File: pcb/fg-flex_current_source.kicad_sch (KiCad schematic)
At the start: 0 parts

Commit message: current sources added
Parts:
- added C13, C14: 0.1uF, Capacitor_THT:C_Disc_D5.1mm_W3.2mm_P5.00mm, symbol Device:C_Small
- added C15: 2.2nF, Capacitor_THT:C_Disc_D5.1mm_W3.2mm_P5.00mm, symbol Device:C_Small
- added Q1: BC547, Package_TO_SOT_THT:TO-92, symbol Transistor_BJT:BC547
- added Q2, Q3: IRF9540N, Package_TO_SOT_THT:TO-220-3_Vertical, symbol Transistor_FET:IRF9540N
- added R10: 0.1R, Resistor_THT:R_Axial_DIN0516_L15.5mm_D5.0mm_P20.32mm_Horizontal, symbol Device:R_Small
- added R11, R4, R5, R6, R7: 1k, Resistor_THT:R_Axial_DIN0207_L6.3mm_D2.5mm_P10.16mm_Horizontal, symbol Device:R_Small
- added R12: 100R, Resistor_THT:R_Axial_DIN0207_L6.3mm_D2.5mm_P10.16mm_Horizontal, symbol Device:R_Small
- added R8, R9: 10k, Resistor_THT:R_Axial_DIN0207_L6.3mm_D2.5mm_P10.16mm_Horizontal, symbol Device:R_Small
- added U6: LM358, Package_DIP:DIP-8_W7.62mm, symbol Amplifier_Operational:LM358
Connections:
- new net: C15.2, R12.1, U6.7
- new net: Q3.1 (G), R12.2
- new net: Q2.2 (D), R10.1
- new net: Q3.3 (S), R10.2, R11.2
- new net -5V: C14.1, U6.4 (V-)
- new net Activation_Signal_FG-Flex: R7.1
- new net GND: C13.2, C14.2, Q1.3 (E), R5.2
- new net I_FG_Flex: Q3.2 (D)
- new net Inv Input U6B: C15.1, R11.1, R6.2, U6.6 (-)
- new net Non-Inv Input U6B: R4.2, R5.1, U6.5 (+)
- new net Q1_Base: Q1.2 (B), R7.2
- new net Q1_Collector: Q1.1 (C), R9.2
- new net Q2_Gate: Q2.1 (G), R8.2, R9.1
- new net U6A Voltage follower: R6.1, U6.1, U6.2 (-)
- new net VCC: C13.1, Q2.3 (S), R4.1, R8.1, U6.8 (V+)
- new net V_{B}: U6.3 (+)

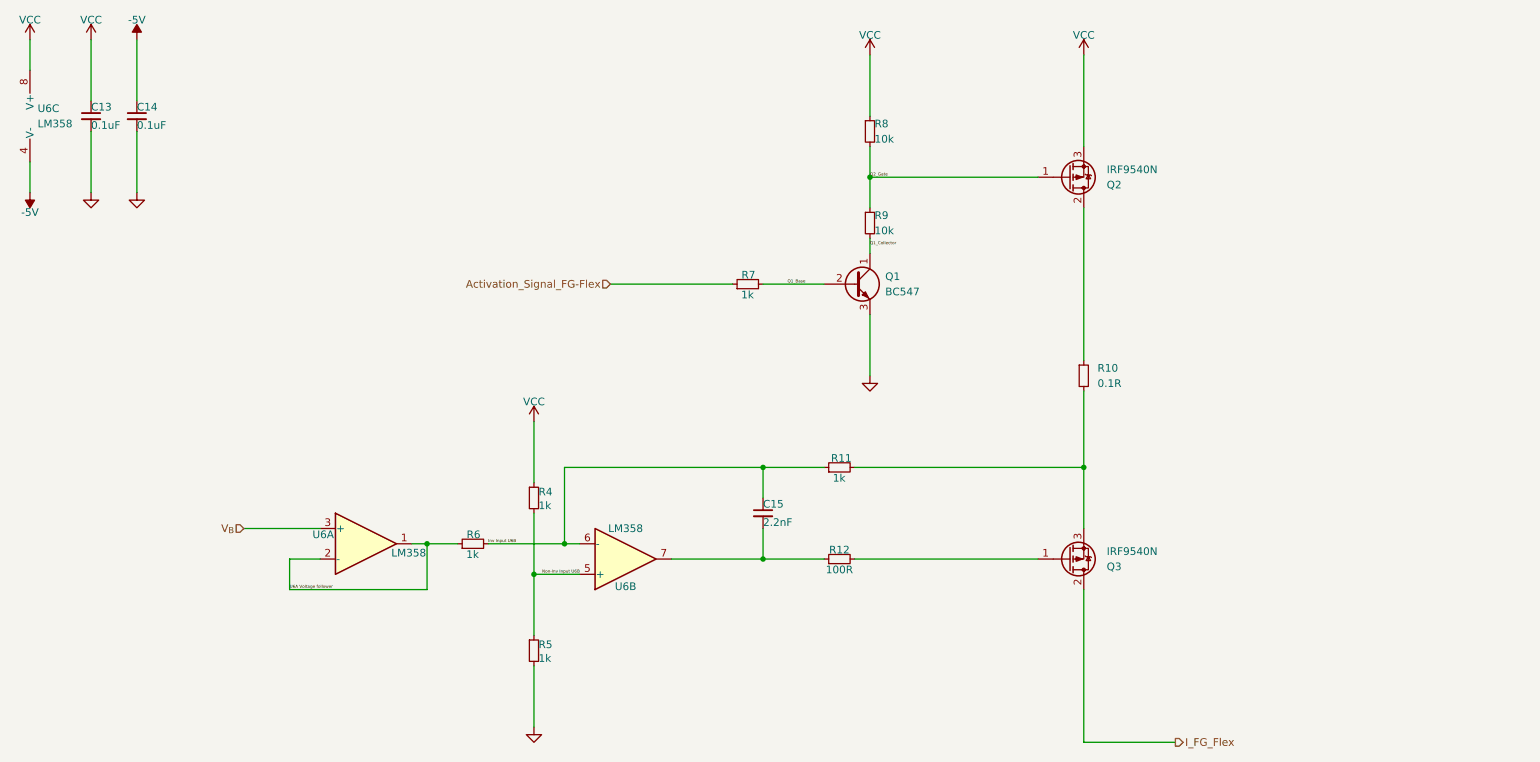
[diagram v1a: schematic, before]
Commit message: shunt measurement changed to different opamp
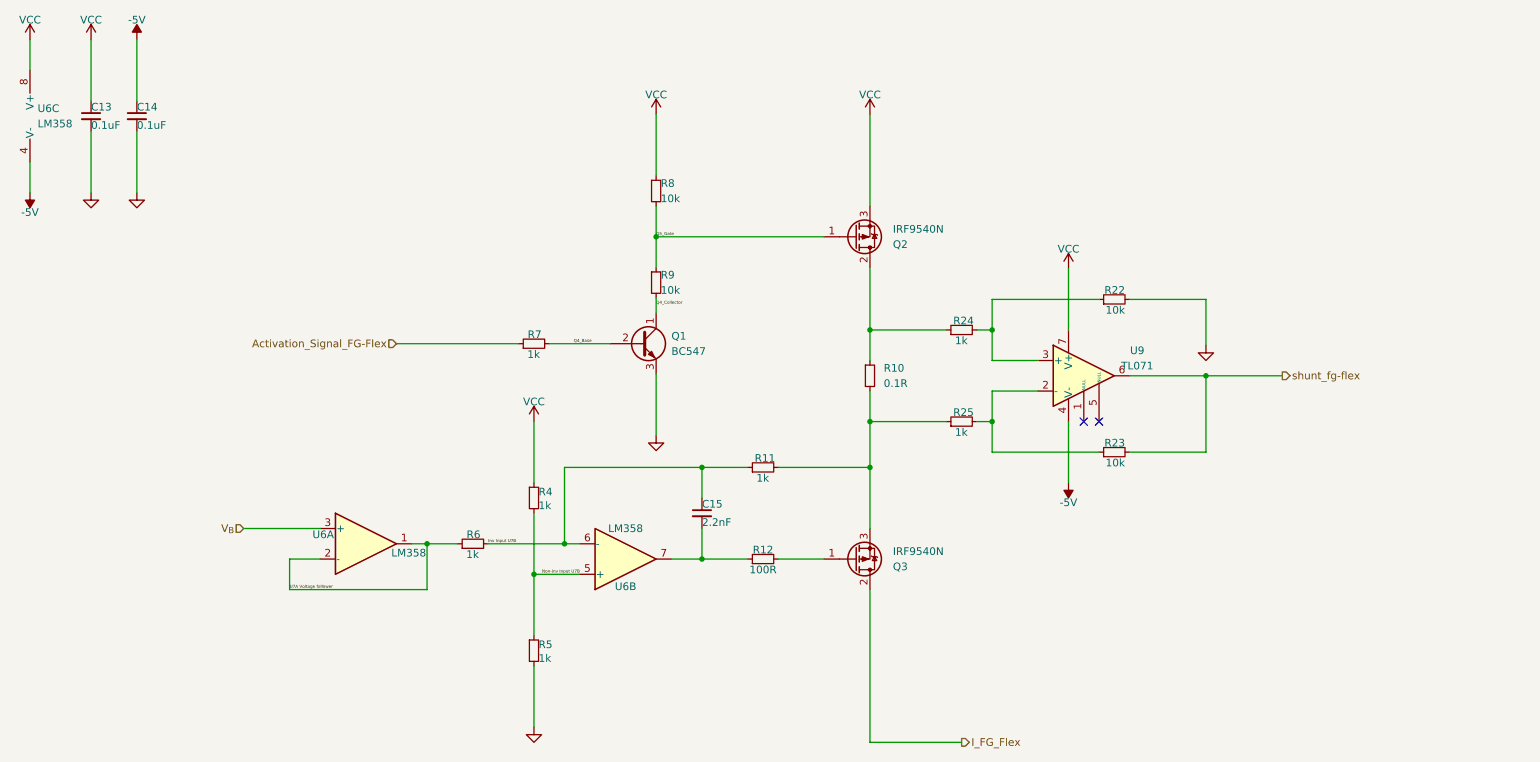
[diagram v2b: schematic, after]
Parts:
- added R22, R23: 10k, Resistor_THT:R_Axial_DIN0207_L6.3mm_D2.5mm_P10.16mm_Horizontal, symbol Device:R_Small
- added R24, R25: 1k, Resistor_THT:R_Axial_DIN0207_L6.3mm_D2.5mm_P10.16mm_Horizontal, symbol Device:R_Small
- added U9: TL071, Package_DIP:DIP-8_W7.62mm, symbol Amplifier_Operational:TL071
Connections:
- net -5V: now also U9.4 (V-)
- net GND: now also R22.2
- net VCC: now also U9.7 (V+)
- net at Q2.2 (D), R10.1: now also R24.1
- net at Q3.3 (S), R10.2, R11.2: now also R25.1
- net Inv Input U6B renamed Inv Input U7B
- net Non-Inv Input U6B renamed Non-Inv Input U7B
- net Q1_Base renamed Q4_Base
- net Q1_Collector renamed Q4_Collector
- net Q2_Gate renamed Q5_Gate
- net U6A Voltage follower renamed U7A Voltage follower
- new net: R23.1, R25.2, U9.2 (-)
- new net: R22.1, R24.2, U9.3 (+)
- new net shunt_fg-flex: R23.2, U9.6
- no-connect marks 0 -> 2
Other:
- moved on the sheet: C15, Q1, Q2, Q3, R10, R11, R12, R7, R8, R9

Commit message: connector added
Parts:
- Q2, Q3: footprint Package_TO_SOT_THT:TO-220-3_Vertical -> Package_TO_SOT_THT:TO-220-3_Horizontal_TabDown
- U6, U9: footprint Package_DIP:DIP-8_W7.62mm -> Package_DIP:DIP-8_W7.62mm_Socket_LongPads
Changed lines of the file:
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@@
       (effects (font (size 1.27 1.27)))
     )
-    (property "Footprint" "Package_DIP:DIP-8_W7.62mm" (at 119.38 111.76 0)
+    (property "Footprint" "Package_DIP:DIP-8_W7.62mm_Socket_LongPads" (at 119.38 111.76 0)
       (effects (font (size 1.27 1.27)) hide)
     )
@@
       (effects (font (size 1.27 1.27)) (justify left))
     )
-    (property "Footprint" "Package_TO_SOT_THT:TO-220-3_Vertical" (at 162.56 56.261 0)
+    (property "Footprint" "Package_TO_SOT_THT:TO-220-3_Horizontal_TabDown" (at 162.56 56.261 0)
       (effects (font (size 1.27 1.27) italic) (justify left) hide)
     )
@@
       (effects (font (size 1.27 1.27)))
     )
-    (property "Footprint" "Package_DIP:DIP-8_W7.62mm" (at 196.85 80.01 0)
+    (property "Footprint" "Package_DIP:DIP-8_W7.62mm_Socket_LongPads" (at 196.85 80.01 0)
       (effects (font (size 1.27 1.27)) hide)
     )
@@
       (effects (font (size 1.27 1.27)) (justify left))
     )
-    (property "Footprint" "Package_TO_SOT_THT:TO-220-3_Vertical" (at 162.56 109.855 0)
+    (property "Footprint" "Package_TO_SOT_THT:TO-220-3_Horizontal_TabDown" (at 162.56 109.855 0)
       (effects (font (size 1.27 1.27) italic) (justify left) hide)
     )
@@
       (effects (font (size 1.27 1.27)))
     )
-    (property "Footprint" "Package_DIP:DIP-8_W7.62mm" (at 76.2 109.22 0)
+    (property "Footprint" "Package_DIP:DIP-8_W7.62mm_Socket_LongPads" (at 76.2 109.22 0)
       (effects (font (size 1.27 1.27)) hide)
     )
@@
       (effects (font (size 1.27 1.27)) (justify left))
     )
-    (property "Footprint" "Package_DIP:DIP-8_W7.62mm" (at 22.86 38.1 0)
-      (effects (font (size 1.27 1.27)) hide)
-    )
+    (property "Footprint" "Package_DIP:DIP-8_W7.62mm_Socket_LongPads" (at 22.86 38.1 0)
+      (effects (font (size 1.27 1.27)) hide)
+    )

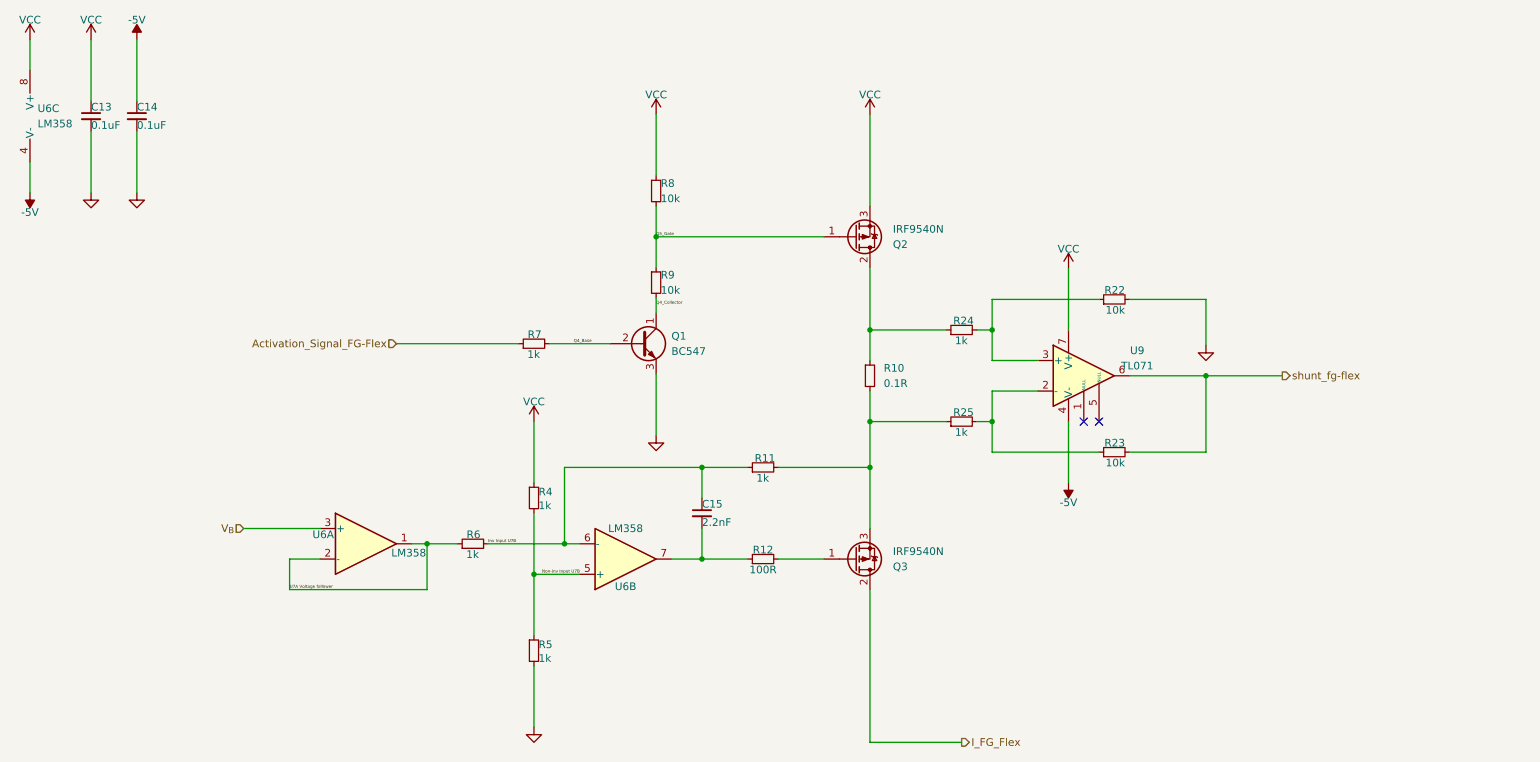
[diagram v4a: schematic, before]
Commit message: vcc changed with +24V
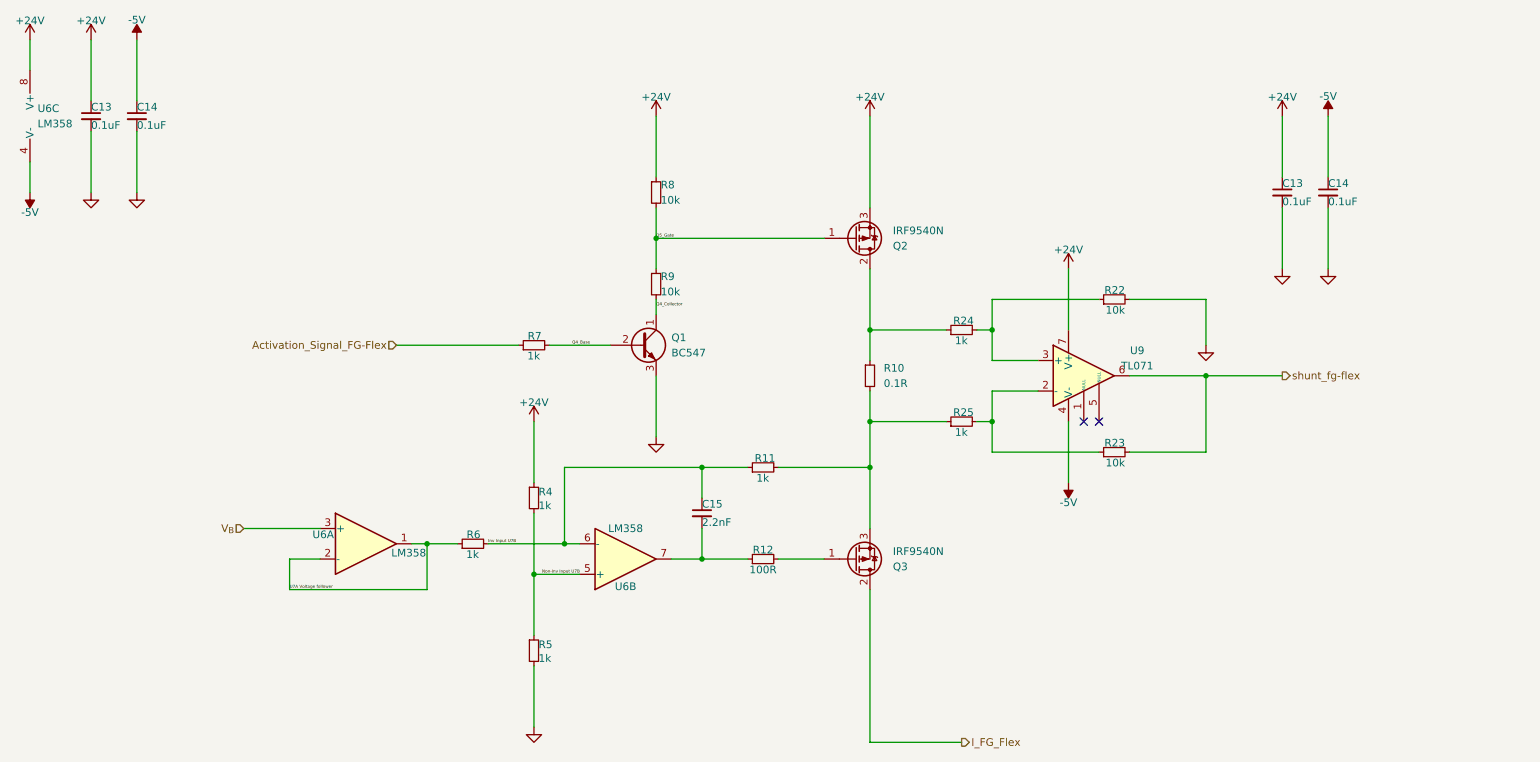
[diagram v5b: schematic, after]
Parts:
- added C13, C14: 0.1uF, Capacitor_THT:C_Disc_D5.1mm_W3.2mm_P5.00mm, symbol Device:C_Small
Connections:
- net -5V: now also C14.1
- net GND: now also C13.2, C14.2
- net VCC renamed +24V
- net +24V: now also C13.1

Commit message: final version schematic?
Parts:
- added D? (x2): 1N5819, Diode_THT:D_DO-41_SOD81_P10.16mm_Horizontal, symbol Diode:1N5819
- added R66: 1k, Resistor_THT:R_Axial_DIN0207_L6.3mm_D2.5mm_P10.16mm_Horizontal, symbol Device:R_Small
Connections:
- net GND: now also D?.2 (A)
- net shunt_fg-flex: now also D?.1 (K), D?.2 (A), R66.2; no longer R23.2, U9.6
- new net: R23.2, R66.1, U9.6
- new net +5V: D?.1 (K)
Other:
- company: (none) -> /dev/tal e.V.
- title: (none) -> FG-Flex Current Source
- moved on the sheet: C13, C14

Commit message: finals in schematic
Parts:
- added J13: Shunt Pin FG Flex, Connector_PinHeader_2.54mm:PinHeader_1x02_P2.54mm_Vertical, symbol Connector:Conn_01x02_Pin
- C13, C14: footprint Capacitor_THT:C_Disc_D5.1mm_W3.2mm_P5.00mm -> Capacitor_THT:C_Disc_D5.0mm_W2.5mm_P2.50mm
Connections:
- net at Q2.2 (D), R10.1, R24.1: now also J13.2 (Pin_2)
- net at Q3.3 (S), R10.2, R11.2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: now also J13.1 (Pin_1)
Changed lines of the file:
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@@
   (junction (at 124.46 58.42) (diameter 0) (color 0 0 0 0)
   )
+  (junction (at 167.64 73.66) (diameter 0) (color 0 0 0 0)
+  )
   (junction (at 104.14 114.3) (diameter 0) (color 0 0 0 0)
   )
@@
   )
   (junction (at 180.34 73.66) (diameter 0) (color 0 0 0 0)
+  )
+  (junction (at 167.64 88.9) (diameter 0) (color 0 0 0 0)
   )
   (junction (at 215.9 81.28) (diameter 0) (color 0 0 0 0)
@@
     (stroke (width 0) (type default))
   )
-  (wire (pts (xy 160.02 88.9) (xy 172.72 88.9))
+  (wire (pts (xy 160.02 88.9) (xy 167.64 88.9))
     (stroke (width 0) (type default))
   )
@@
     (stroke (width 0) (type default))
   )
+  (wire (pts (xy 167.64 73.66) (xy 172.72 73.66))
+    (stroke (width 0) (type default))
+  )
+  (wire (pts (xy 167.64 88.9) (xy 172.72 88.9))
+    (stroke (width 0) (type default))
+  )
   (wire (pts (xy 215.9 81.28) (xy 228.6 81.28))
     (stroke (width 0) (type default))
@@
     (stroke (width 0) (type default))
   )
+  (wire (pts (xy 167.64 80.01) (xy 167.64 73.66))
+    (stroke (width 0) (type default))
+  )
   (wire (pts (xy 109.22 109.22) (xy 111.76 109.22))
     (stroke (width 0) (type default))
   )
-  (wire (pts (xy 160.02 73.66) (xy 172.72 73.66))
+  (wire (pts (xy 170.18 82.55) (xy 167.64 82.55))
+    (stroke (width 0) (type default))
+  )
+  (wire (pts (xy 160.02 73.66) (xy 167.64 73.66))
     (stroke (width 0) (type default))
   )
@@
     (stroke (width 0) (type default))
   )
+  (wire (pts (xy 167.64 82.55) (xy 167.64 88.9))
+    (stroke (width 0) (type default))
+  )
   (wire (pts (xy 187.96 78.74) (xy 180.34 78.74))
     (stroke (width 0) (type default))
@@
   )
   (wire (pts (xy 215.9 93.98) (xy 215.9 81.28))
+    (stroke (width 0) (type default))
+  )
+  (wire (pts (xy 170.18 80.01) (xy 167.64 80.01))
     (stroke (width 0) (type default))
   )
@@
       (effects (font (size 1.27 1.27)) (justify left))
     )
-    (property "Footprint" "Capacitor_THT:C_Disc_D5.1mm_W3.2mm_P5.00mm" (at 38.1 38.1 0)
+    (property "Footprint" "Capacitor_THT:C_Disc_D5.0mm_W2.5mm_P2.50mm" (at 38.1 38.1 0)
       (effects (font (size 1.27 1.27)) hide)
     )
@@
         (path "/6ce7d73a-8297-412b-a1cf-6113d41486fd/1320187d-24fd-4fe0-8f0e-0b43909d8592"
           (reference "C26") (unit 1)
+        )
+      )
+    )
+  )
+  (symbol (lib_id "Connector:Conn_01x02_Pin") (at 175.26 82.55 180) (unit 1)
+    (in_bom yes) (on_board yes) (dnp no)
+    (property "Reference" "J13" (at 176.53 80.01 0)
+      (effects (font (size 1.27 1.27)) (justify right))
+    )
+    (property "Value" "Shunt Pin FG Flex" (at 170.18 85.09 0)
+      (effects (font (size 1.27 1.27)) (justify right))
+    )
+    (property "Footprint" "Connector_PinHeader_2.54mm:PinHeader_1x02_P2.54mm_Vertical" (at 175.26 82.55 0)
+      (effects (font (size 1.27 1.27)) hide)
+    )
+    (property "Datasheet" "~" (at 175.26 82.55 0)
+      (effects (font (size 1.27 1.27)) hide)
+    )
+    (pin "2")
+    (pin "1")
+    (instances
+      (project "fg_lampe"
+        (path "/6ce7d73a-8297-412b-a1cf-6113d41486fd/ba76f9dc-1045-4df8-971c-12fc9c8a3a7f"
+          (reference "J13") (unit 1)
+        )
+        (path "/6ce7d73a-8297-412b-a1cf-6113d41486fd/1320187d-24fd-4fe0-8f0e-0b43909d8592"
+          (reference "J14") (unit 1)
         )
       )
@@
       (effects (font (size 1.27 1.27)) (justify left))
     )
-    (property "Footprint" "Capacitor_THT:C_Disc_D5.1mm_W3.2mm_P5.00mm" (at 215.9 48.26 0)
+    (property "Footprint" "Capacitor_THT:C_Disc_D5.0mm_W2.5mm_P2.50mm" (at 215.9 48.26 0)
       (effects (font (size 1.27 1.27)) hide)
     )
@@
       (effects (font (size 1.27 1.27)) (justify left))
     )
-    (property "Footprint" "Capacitor_THT:C_Disc_D5.1mm_W3.2mm_P5.00mm" (at 208.28 48.26 0)
+    (property "Footprint" "Capacitor_THT:C_Disc_D5.0mm_W2.5mm_P2.50mm" (at 208.28 48.26 0)
       (effects (font (size 1.27 1.27)) hide)
     )
@@
       (effects (font (size 1.27 1.27)) (justify left))
     )
-    (property "Footprint" "Capacitor_THT:C_Disc_D5.1mm_W3.2mm_P5.00mm" (at 30.48 38.1 0)
-      (effects (font (size 1.27 1.27)) hide)
-    )
+    (property "Footprint" "Capacitor_THT:C_Disc_D5.0mm_W2.5mm_P2.50mm" (at 30.48 38.1 0)
+      (effects (font (size 1.27 1.27)) hide)
+    )
